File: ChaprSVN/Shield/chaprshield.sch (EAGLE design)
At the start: 12 parts

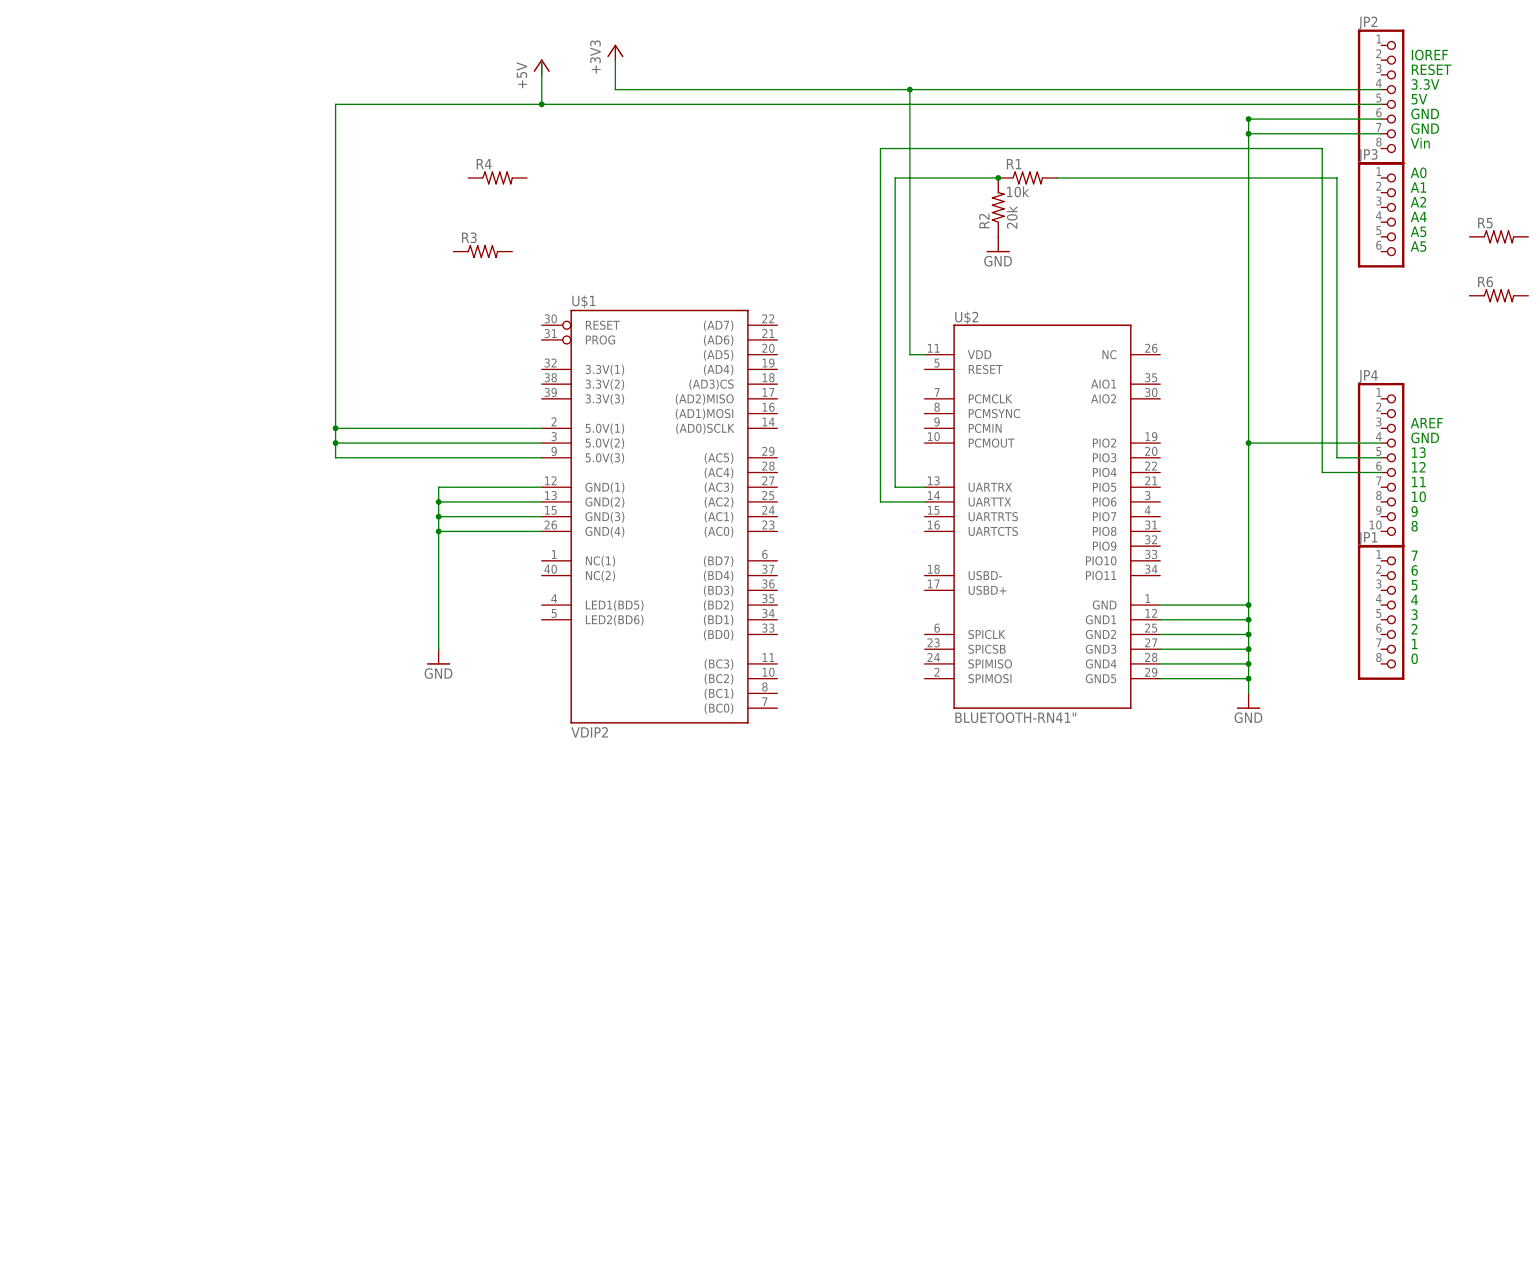
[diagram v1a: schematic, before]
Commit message: 
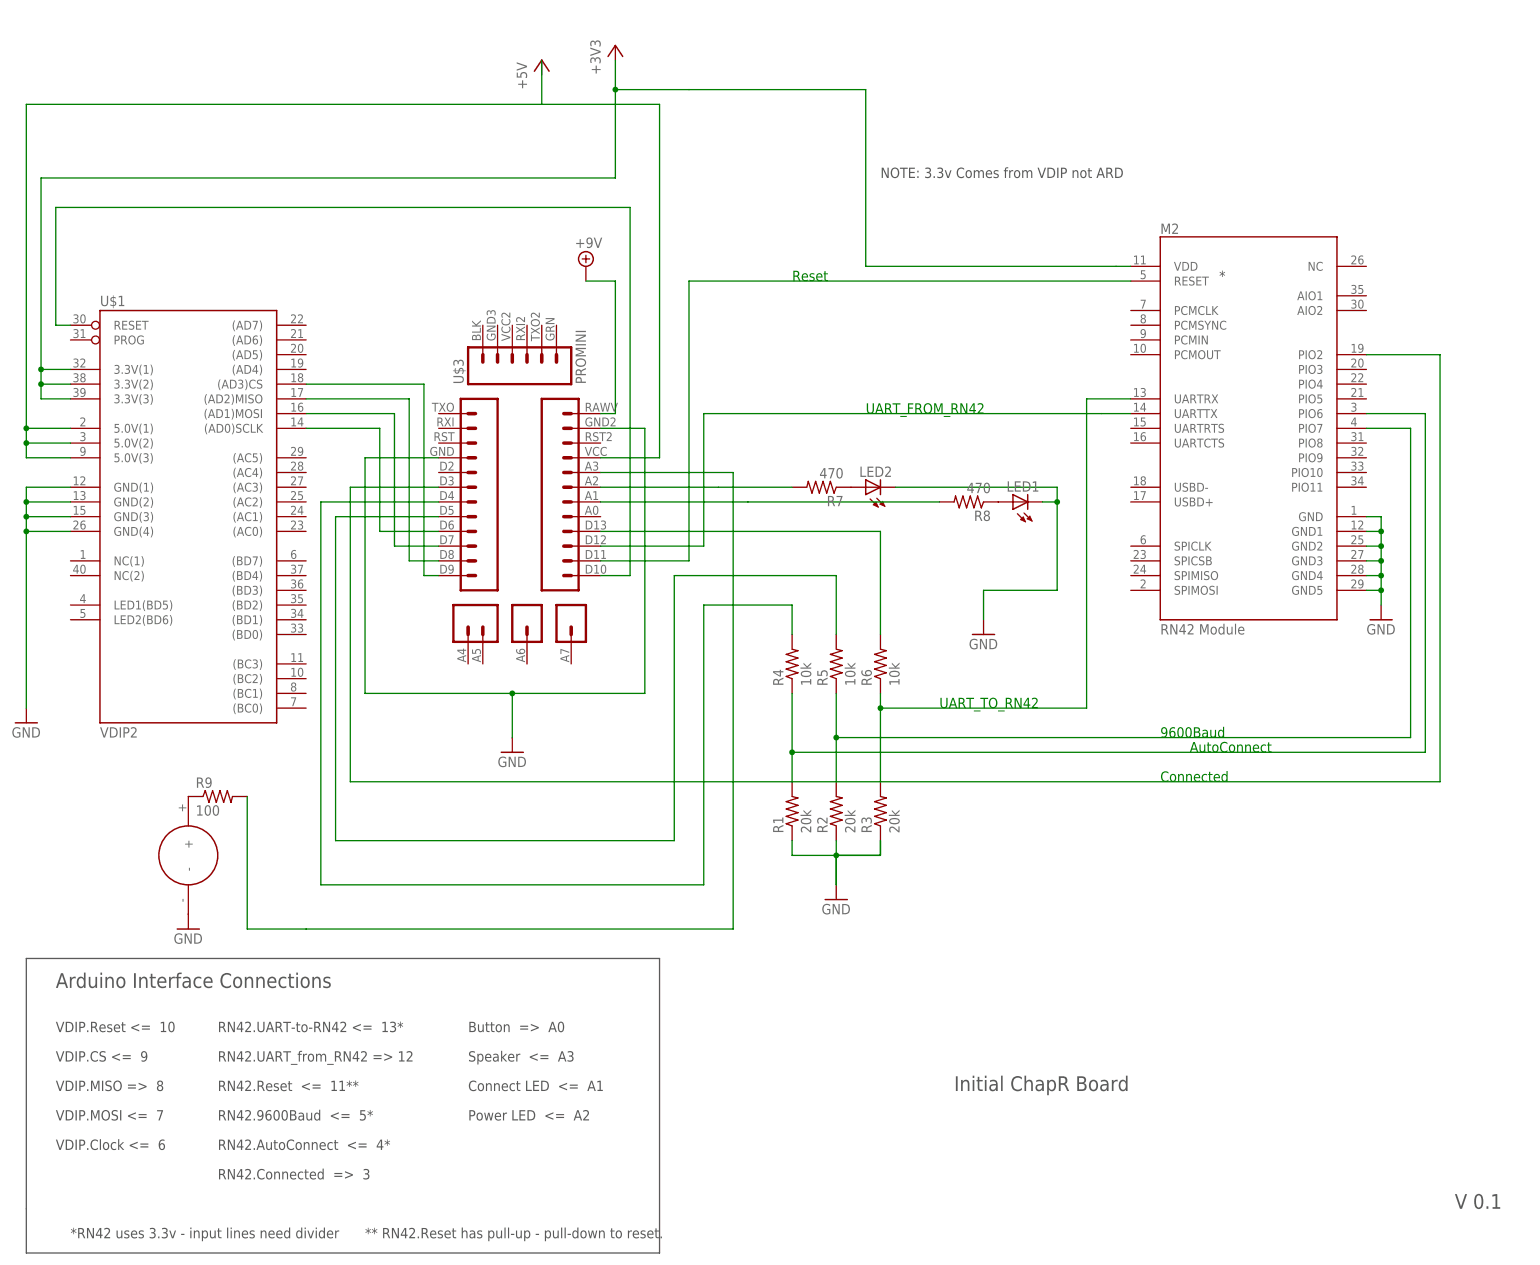
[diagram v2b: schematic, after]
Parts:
- removed JP1, JP2: (no value), pinhead:PINHD-1X8
- removed JP3: (no value), pinhead:PINHD-1X6
- removed JP4: (no value), pinhead:PINHD-1X10
- added LED1, LED2: (no value), led:LED3MM
- added M2: RN42 Module, SparkFun-RF:BLUETOOTH-RN41"
- added R7, R8: 470, resistor:R-US_0207/10
- added R9: 100, resistor:R-US_0207/10
- added U$3: PROMINI, ChapR-Custom:PROMINI
- R1: value 10k -> 20k
- R3: value (none) -> 20k
- R4, R5, R6: value (none) -> 10k
- U$2: value BLUETOOTH-RN41" -> SPEAKER; device SparkFun-RF:BLUETOOTH-RN41" -> ChapR-Custom:SPEAKER
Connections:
- new net +9V: U$3.RAWV
- new net 3.3V: M2.VDD, U$1.3.3V(1), U$1.3.3V(2), U$1.3.3V(3)
- new net N$10: U$1.(AD3)CS, U$3.D9
- new net N$11: U$1.(AD2)MISO, U$3.D8
- new net N$12: U$1.(AD1)MOSI, U$3.D7
- new net N$13: U$1.(AD0)SCLK, U$3.D6
- new net N$14: R4.2, U$3.D4
- new net N$15: M2.PIO2, U$3.D3
- new net N$16: LED2.A, R7.1
- new net N$17: LED1.A, R8.1
- new net N$18: R7.2, U$3.A2
- new net N$19: R9.1, U$2.+
- new net N$20: R8.2, U$3.A1
- new net N$21: R9.2, U$3.A3
- new net N$6: M2.PIO6, R1.2, R4.1
- new net N$7: M2.PIO7, R2.2, R5.1
- new net N$8: R5.2, U$3.D5
- new net N$9: M2.UARTRX, R3.2, R6.1
- net GND: now also LED1.C, LED2.C, M2.GND, M2.GND1, M2.GND2, M2.GND3, M2.GND4, M2.GND5, R1.1, R3.1, U$2.-, U$3.GND, U$3.GND2; no longer JP2.6, JP2.7, JP4.4, U$2.GND, U$2.GND1, U$2.GND2, U$2.GND3, U$2.GND4, U$2.GND5
- net N$1: now also U$3.VCC; no longer JP2.5
- net N$2: now also U$1.RESET, U$3.D10; no longer JP2.4, U$2.VDD
- net N$3: now also R6.2, U$3.D13; no longer JP4.5, R1.2
- net N$4: now also M2.UARTTX, U$3.D12; no longer R1.1, R2.2, U$2.UARTRX
- net N$5: now also M2.RESET, U$3.D11; no longer JP4.6, U$2.UARTTX
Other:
- note added: "*"
- note added: "** RN42.Reset has pull-up - pull-down to reset."
- note added: "*RN42 uses 3.3v - input lines need divider"
- note added: "9600Baud"
- note added: "Arduino Interface Connections"
- note added: "AutoConnect"
- note added: "Button => A0"
- note added: "Connect LED <= A1"
- note added: "Connected"
- note added: "Initial ChapR Board"
- note added: "NOTE: 3.3v Comes from VDIP not ARD"
- note added: "Power LED <= A2"
- note added: "RN42.9600Baud <= 5*"
- note added: "RN42.AutoConnect <= 4*"
- note added: "RN42.Connected => 3"
- note added: "RN42.Reset <= 11**"
- note added: "RN42.UART-to-RN42 <= 13*"
- note added: "RN42.UART_from_RN42 => 12"
- note added: "Reset"
- note added: "Speaker <= A3"
- note added: "UART_FROM_RN42"
- note added: "UART_TO_RN42"
- note added: "V 0.1"
- note added: "VDIP.CS <= 9"
- note added: "VDIP.Clock <= 6"
- note added: "VDIP.MISO => 8"
- note added: "VDIP.MOSI <= 7"
- note added: "VDIP.Reset <= 10"
- note removed: "0"
- note removed: "1"
- note removed: "10"
- note removed: "11"
- note removed: "12"
- note removed: "13"
- note removed: "2"
- note removed: "3"
- note removed: "3.3V"
- note removed: "4"
- note removed: "5"
- note removed: "5V"
- note removed: "6"
- note removed: "7"
- note removed: "8"
- note removed: "9"
- note removed: "A0"
- note removed: "A1"
- note removed: "A2"
- note removed: "A4"
- note removed: "A5"
- note removed: "AREF"
- note removed: "GND"
- note removed: "IOREF"
- note removed: "RESET"
- note removed: "Vin"
- moved on the sheet: R1, R2, R3, R4, R5, R6, U$1

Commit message: added power connector, placed holes
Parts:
- added -: 9v power, con-molex:22-23-2021
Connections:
- net +9V: now also --2.S
- net GND: now also --1.S
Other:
- note added: "+"
- note added: "-"
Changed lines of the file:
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@@
 <part name="R9" library="resistor" deviceset="R-US_" device="0207/10" value="100"/>
 <part name="GND7" library="supply1" deviceset="GND" device=""/>
+<part name="-" library="con-molex" deviceset="22-23-2021" device="" value="9v power"/>
+<part name="GND6" library="supply1" deviceset="GND" device=""/>
 </parts>
 <sheets>
@@
 <wire x1="25.4" y1="-25.4" x2="25.4" y2="-76.2" width="0.1524" layer="97"/>
 <wire x1="25.4" y1="-76.2" x2="-83.82" y2="-76.2" width="0.1524" layer="97"/>
-<wire x1="-83.82" y1="-76.2" x2="-83.82" y2="-68.58" width="0.1524" layer="97"/>
-<wire x1="-83.82" y1="-68.58" x2="-83.82" y2="-25.4" width="0.1524" layer="97"/>
+<wire x1="-83.82" y1="-76.2" x2="-83.82" y2="-25.4" width="0.1524" layer="97"/>
 <text x="-78.74" y="-30.48" size="2.54" layer="97">Arduino Interface Connections</text>
 <text x="-78.74" y="-38.1" size="1.778" layer="97">VDIP.Reset &lt;=  10</text>
@@
 <text x="-7.62" y="-53.34" size="1.778" layer="97">Power LED  &lt;=  A2</text>
 <text x="111.76" y="5.08" size="1.778" layer="91">Connected</text>
+<text x="-22.098" y="92.964" size="1.778" layer="91">+</text>
+<text x="-22.098" y="96.012" size="1.778" layer="91">-</text>
 </plain>
 <instances>
@@
 <instance part="R9" gate="G$1" x="-50.8" y="2.54"/>
 <instance part="GND7" gate="1" x="-55.88" y="-20.32"/>
+<instance part="-" gate="-1" x="-17.78" y="96.52" smashed="yes" rot="MR0">
+<attribute name="VALUE" x="-17.018" y="97.917" size="1.778" layer="96" rot="MR0"/>
+</instance>
+<instance part="-" gate="-2" x="-17.78" y="93.98" smashed="yes" rot="MR0"/>
+<instance part="GND6" gate="1" x="-25.4" y="86.36"/>
 </instances>
 <busses>
@@
 <pinref part="GND7" gate="1" pin="GND"/>
 </segment>
+<segment>
+<pinref part="-" gate="-1" pin="S"/>
+<wire x1="-15.24" y1="96.52" x2="-15.24" y2="101.6" width="0.1524" layer="91"/>
+<wire x1="-15.24" y1="101.6" x2="-33.02" y2="101.6" width="0.1524" layer="91"/>
+<wire x1="-33.02" y1="101.6" x2="-33.02" y2="88.9" width="0.1524" layer="91"/>
+<pinref part="GND6" gate="1" pin="GND"/>
+<wire x1="-33.02" y1="88.9" x2="-25.4" y2="88.9" width="0.1524" layer="91"/>
+</segment>
 </net>
 <net name="N$1" class="0">
@@
 <pinref part="U$3" gate="G$1" pin="RAWV"/>
 <wire x1="17.78" y1="68.58" x2="15.24" y2="68.58" width="0.1524" layer="91"/>
-</segment>
-</net>
+<pinref part="-" gate="-2" pin="S"/>
+<wire x1="-15.24" y1="93.98" x2="-15.24" y2="91.44" width="0.1524" layer="91"/>
+<wire x1="-15.24" y1="91.44" x2="12.7" y2="91.44" width="0.1524" layer="91"/>
+<junction x="12.7" y="91.44"/>
+</segment>
+</net>

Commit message: First version of the ChapR board v0.2.  These files were sent to Sunstone.
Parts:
- added JP1: (no value), pinhead:PINHD-1X2
- added PB1: PUSHBUTTON, ChapR-Custom:PUSHBUTTON
- added R10, R11: 10k, resistor:R-US_0207/10
- renumbered U$1 to VDIP, U$3 to ARD
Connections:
- new net N$22: JP1.1, M2.PIO4, R11.2
- new net N$24: ARD.A0, PB1.2, R10.2
- net 3.3V: now also JP1.2
- net GND: now also R10.1, R11.1; no longer M2.GND2, M2.GND3
- net N$1: now also PB1.1
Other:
- note added: "Factory Reset"

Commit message: 
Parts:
- R1, R2, R3: value 20k -> 19.1k
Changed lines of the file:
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@@
 <part name="+3V1" library="supply1" deviceset="+3V3" device=""/>
 <part name="P+1" library="supply1" deviceset="+5V" device=""/>
-<part name="R1" library="resistor" deviceset="R-US_" device="0207/10" value="20k"/>
-<part name="R2" library="resistor" deviceset="R-US_" device="0207/10" value="20k"/>
-<part name="R3" library="resistor" deviceset="R-US_" device="0207/10" value="20k"/>
+<part name="R1" library="resistor" deviceset="R-US_" device="0207/10" value="19.1k"/>
+<part name="R2" library="resistor" deviceset="R-US_" device="0207/10" value="19.1k"/>
+<part name="R3" library="resistor" deviceset="R-US_" device="0207/10" value="19.1k"/>
 <part name="R4" library="resistor" deviceset="R-US_" device="0207/10" value="10k"/>
 <part name="R5" library="resistor" deviceset="R-US_" device="0207/10" value="10k"/>
